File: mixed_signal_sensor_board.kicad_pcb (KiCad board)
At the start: 4 copper layers, 85 x 58 mm, 159 parts, among them J1 Conn_01x02, J10 Conn_01x04, J11 Conn_01x04, J12 Conn_01x04, J13 USB_C_Receptacle_USB2.0_16P, J14 Conn_01x04, J15 PYRO, J16 PYRO, J17 PYRO, J18 PYRO, J2 Conn_01x04, J3 Conn_01x06, J4 Conn_02x06_Odd_Even, J5 Conn_01x04, J6 Conn_01x04, J7 Conn_01x04, J8 Conn_01x04, J9 Conn_01x04, Q1 IRLML5103TRPBF, Q2 CSD17571Q2, Q3 CSD17571Q2, Q4 CSD17571Q2, Q5 CSD17571Q2, SW1 SW_Push, SW2 SW_Push, U1 TMP117xxDRV, U2 LM27762, U3 MagI3C_171013201, U4 TPS7A20xxxDBV, U5 TPS7A20xxxDBV, U6 ADS131M08xPBS, U7 STM32L552CEUx, U8 USBLC6-2P6, U9 TCAN3414DRBR, Y1 SG-8018CE_8.192M-TJHSA

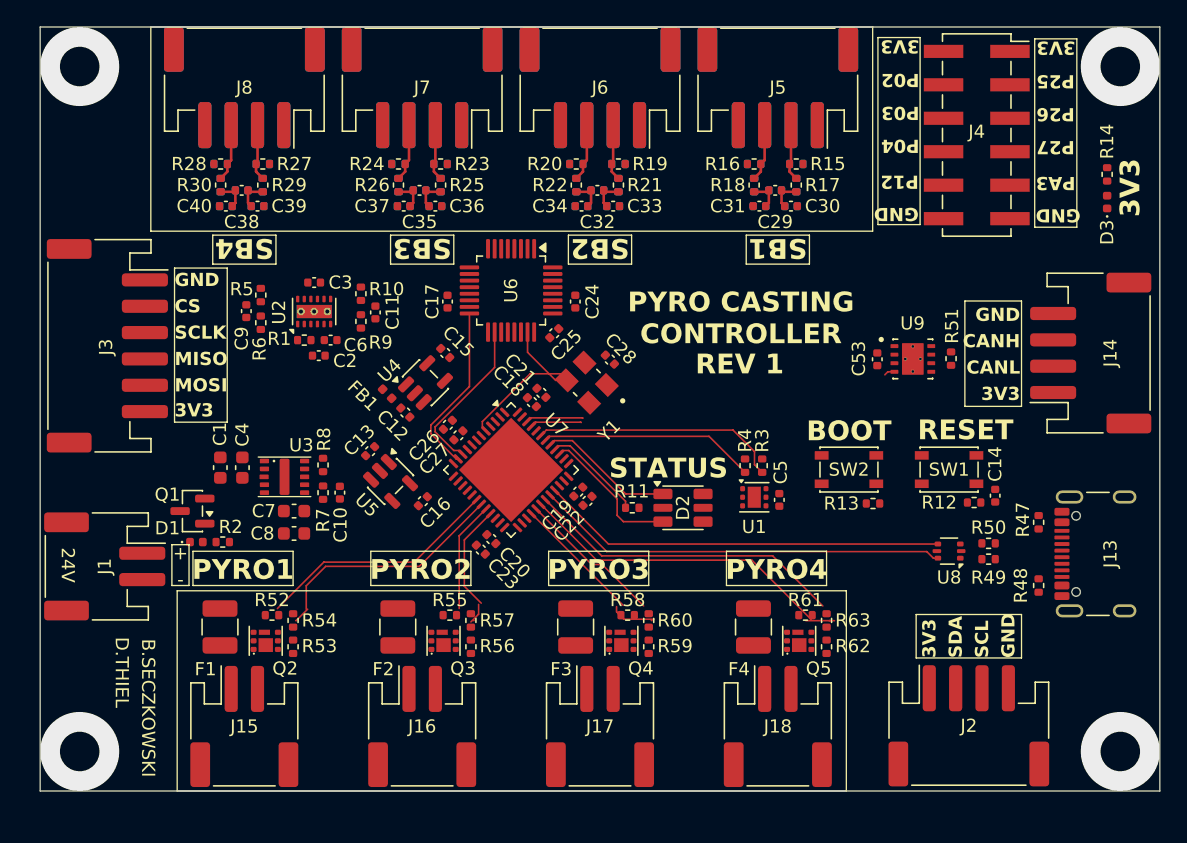
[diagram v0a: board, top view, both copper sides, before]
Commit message: removed SPI, I2C, compacting pyro channels, new pyro schematic
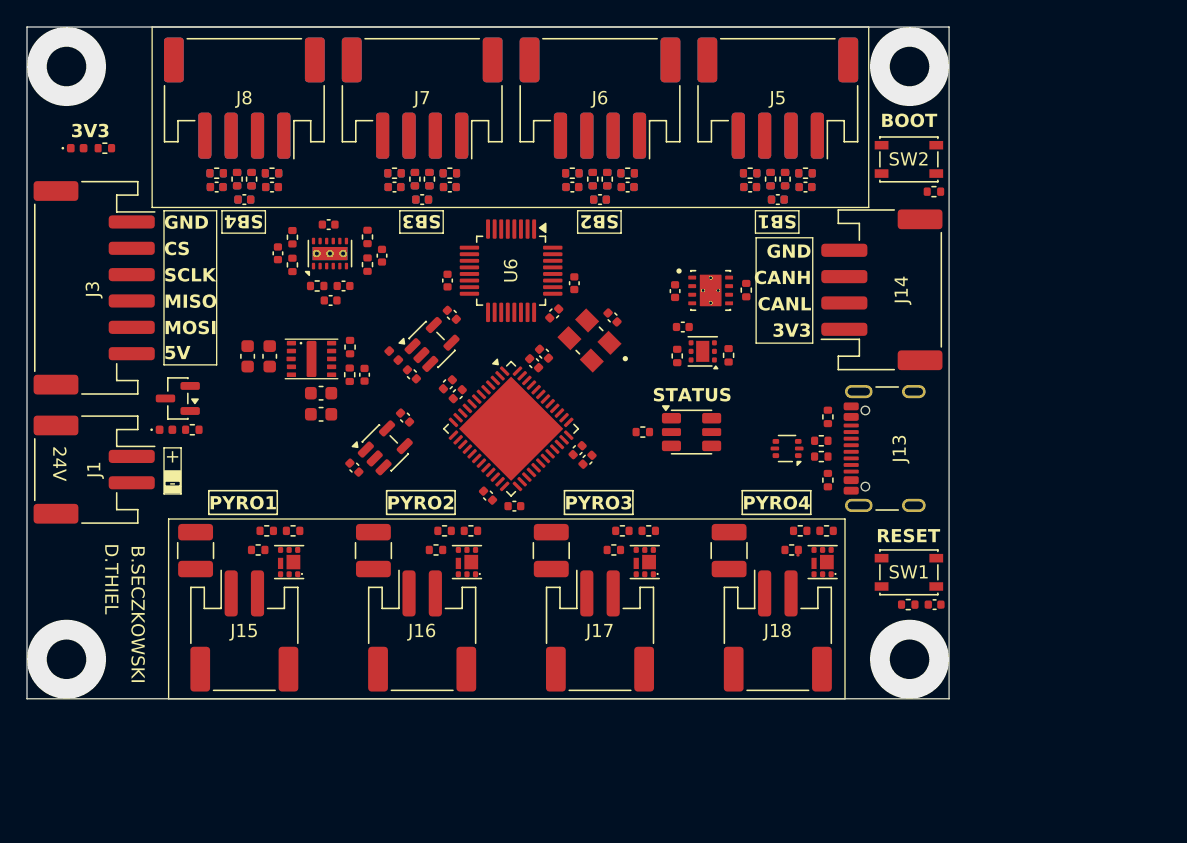
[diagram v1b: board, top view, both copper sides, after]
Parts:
- removed J2: Conn_01x04, Connector_JST:JST_PH_S4B-PH-SM4-TB_1x04-1MP_P2.00mm_Horizontal
- removed J4: Conn_02x06_Odd_Even, Connector_PinSocket_2.54mm:PinSocket_2x06_P2.54mm_Vertical_SMD
- moved D3 78.3 mm to (123.8, 61.2), turned to 0 degrees
- moved R14 76.1 mm to (125.9, 61.2), turned to 0 degrees
- moved R13 24.1 mm to (188.8, 64.5)
- moved SW2 24.0 mm to (186.9, 62.0)
- moved J13 17.9 mm to (186.2, 84.0)
- moved R47 17.9 mm to (180.8, 81.6)
- moved R48 17.9 mm to (180.8, 86.4)
- moved J14 16.6 mm to (184.9, 72.0)
- moved R51 16.4 mm to (174.6, 72.0)
- moved U9 16.2 mm to (171.9, 72.0)
- moved C53 16.2 mm to (169.2, 72.0)
- moved C5 15.0 mm to (169.8, 74.8), turned to 0 degrees
- moved R49 14.9 mm to (180.3, 84.6)
- moved R50 14.9 mm to (180.3, 83.4)
- moved U8 14.6 mm to (177.7, 84.0)
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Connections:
- U7 pad 10: /ADS_DRDY -> unconnected-(U7-PA0-Pad10)
- U7 pad 11: /ADS_SYNC/RESET -> unconnected-(U7-PA1-Pad11)
- U7 pad 12: /PA2 -> unconnected-(U7-PA2-Pad12)
- U7 pad 13: /PA3 -> unconnected-(U7-PA3-Pad13)
- U7 pad 2: /PC13 -> /ADS_DRDY
- U7 pad 25: /PB12 -> unconnected-(U7-PB12-Pad25)
- U7 pad 26: /PB13 -> unconnected-(U7-PB13-Pad26)
- U7 pad 27: /PB14 -> unconnected-(U7-PB14-Pad27)
- U7 pad 3: /PC14 -> /ADS_SYNC/RESET
- U7 pad 4: /PC15 -> unconnected-(U7-PC15-Pad4)
- U7 pad 5: /CLK_IN -> unconnected-(U7-PH0-Pad5)
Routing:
- net /USB_N: track 31.4 -> 0.00 mm
- net /USB_P: track 30.8 -> 0.00 mm
- net /PYRO4_FAULT: track 26.4 -> 0.00 mm
- net /PYRO4_SIGNAL: track 24.4 -> 0.06 mm
- net /PYRO1_FAULT: track 18.9 -> 0.00 mm
- net /SDA: track 18.9 -> 0.00 mm
- net /PYRO1_SIGNAL: track 18.6 -> 0.06 mm
- net /SCL: track 16.4 -> 0.00 mm
- net /CLK_IN: track 14.3 -> 0.00 mm
- net /PYRO3_FAULT: track 13.4 -> 0.00 mm
- net /ADS_SYNC/RESET: track 13.2 -> 0.00 mm
- net /ADS_DRDY: track 12.2 -> 0.00 mm
- net /PYRO3_SIGNAL: track 11.2 -> 0.06 mm
- net /LEDG: track 10.9 -> 0.00 mm
- net /LEDB: track 10.4 -> 0.00 mm
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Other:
- board size 85 x 58 mm -> 70 x 51 mm
- board text added: "5V"
- board text removed: "P02"
- board text removed: "P03"
- board text removed: "P04"
- board text removed: "P12"
- board text removed: "P25"
- board text removed: "P26"
- board text removed: "P27"
- board text removed: "PA3"
- board text removed: "PYRO CASTING CONTROLLER"
- board text removed: "REV 1"
- board text removed: "SCL"
- board text removed: "SDA"

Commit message: New pyro layout, SWDIO, SWCLK, USART2 TX RX, 70x50mm board
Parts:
- removed F1, F2, F3, F4: Polyfuse, Fuse:Fuse_1210_3225Metric
- removed J15, J16, J17, J18: PYRO, Connector_JST:JST_PH_S2B-PH-SM4-TB_1x02-1MP_P2.00mm_Horizontal
- removed R52, R54, R55, R57, R58, R60, R61, R63: 10K, Resistor_SMD:R_0402_1005Metric
- removed R53, R56, R59, R62: 70K, Resistor_SMD:R_0402_1005Metric
- added 50k1: 10K, Resistor_SMD:R_0402_1005Metric, F.Cu at (147.6, 92.2)
- added D4: 3V, Diode_SMD:D_0402_1005Metric, F.Cu at (149.3, 96.2)
- added D5: 3V, Diode_SMD:D_0402_1005Metric, F.Cu at (159.8, 96.2)
- added D6: 3V, Diode_SMD:D_0402_1005Metric, F.Cu at (170.3, 96.2)
- added D7: 3V, Diode_SMD:D_0402_1005Metric, F.Cu at (180.8, 96.2)
- added F5: Polyfuse, Fuse:Fuse_1210_3225Metric, F.Cu at (140.6, 90.7)
- added F6: Polyfuse, Fuse:Fuse_1210_3225Metric, F.Cu at (151.1, 90.7)
- added F7: Polyfuse, Fuse:Fuse_1210_3225Metric, F.Cu at (161.6, 90.7)
- added F8: Polyfuse, Fuse:Fuse_1210_3225Metric, F.Cu at (172.1, 90.7)
- added J19: PYRO, Connector_JST:JST_PH_S2B-PH-SM4-TB_1x02-1MP_P2.00mm_Horizontal, F.Cu at (144.2, 96.8)
- added J20: PYRO, Connector_JST:JST_PH_S2B-PH-SM4-TB_1x02-1MP_P2.00mm_Horizontal, F.Cu at (154.8, 96.8)
- added J21: PYRO, Connector_JST:JST_PH_S2B-PH-SM4-TB_1x02-1MP_P2.00mm_Horizontal, F.Cu at (165.2, 96.8)
- added J22: PYRO, Connector_JST:JST_PH_S2B-PH-SM4-TB_1x02-1MP_P2.00mm_Horizontal, F.Cu at (175.8, 96.8)
- added J23: PYRO_ARM, Connector_JST:JST_PH_S2B-PH-SM4-TB_1x02-1MP_P2.00mm_Horizontal, F.Cu at (133.8, 96.8)
- added Q10: CSD17571Q2, CSD17571Q2:CSD17571Q2, F.Cu at (147.8, 90.2)
- added Q11: CSD17571Q2, CSD17571Q2:CSD17571Q2, F.Cu at (158.3, 90.2)
- added Q12: CSD17571Q2, CSD17571Q2:CSD17571Q2, F.Cu at (168.8, 90.2)
- added Q13: CSD17571Q2, CSD17571Q2:CSD17571Q2, F.Cu at (179.3, 90.2)
- added R72: 50K, Resistor_SMD:R_0402_1005Metric, F.Cu at (149.3, 94.0)
- added R74: 50K, Resistor_SMD:R_0402_1005Metric, F.Cu at (159.8, 94.0)
- added R75: 10K, Resistor_SMD:R_0402_1005Metric, F.Cu at (158.1, 92.2)
- added R76: 50K, Resistor_SMD:R_0402_1005Metric, F.Cu at (170.3, 94.0)
- added R77: 10K, Resistor_SMD:R_0402_1005Metric, F.Cu at (168.6, 92.2)
- added R78: 50K, Resistor_SMD:R_0402_1005Metric, F.Cu at (180.8, 94.0)
- added R79: 10K, Resistor_SMD:R_0402_1005Metric, F.Cu at (179.1, 92.2)
- added R80: 100k, Resistor_SMD:R_0402_1005Metric, F.Cu at (147.5, 88.2)
- added R81: 100k, Resistor_SMD:R_0402_1005Metric, F.Cu at (158.0, 88.2)
- added R82: 100k, Resistor_SMD:R_0402_1005Metric, F.Cu at (168.5, 88.2)
- added R83: 100k, Resistor_SMD:R_0402_1005Metric, F.Cu at (179.0, 88.2)
- D1: value 30V -> 24V
- Q2, Q3, Q4, Q5: value CSD17571Q2 -> IRLML5103TRPBF; footprint CSD17571Q2:CSD17571Q2 -> Package_TO_SOT_SMD:SOT-23
- moved D3 48.7 mm to (171.9, 68.6), turned to 180 degrees
- moved R14 44.6 mm to (169.9, 68.6)
- moved C14 7.27 mm to (184.7, 90.0), turned to 180 degrees
- moved R12 5.91 mm to (186.7, 90.0), turned to 180 degrees
- moved D1 5.64 mm to (132.9, 87.7)
- moved R2 5.64 mm to (134.9, 87.7)
- moved Q5 5.55 mm to (175.8, 89.6), turned to -90 degrees
- moved Q2 5.30 mm to (144.2, 89.6), turned to -90 degrees
- moved C13 4.34 mm to (147.3, 81.9), turned to 90 degrees
- moved Q1 4.05 mm to (133.8, 83.5)
- moved C16 4.01 mm to (152.7, 81.9), turned to -90 degrees
- moved C20 3.93 mm to (158.2, 85.3)
- moved U7 3.87 mm to (160.0, 80.4)
- moved C26 3.86 mm to (155.2, 77.0)
- moved C27 3.86 mm to (155.9, 77.8)
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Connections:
- D1 pad 1: Net-(D1-K) -> +24V
- J1 pad 1: Net-(D1-K) -> Net-(J1-Pin_1)
- J3 pad 2: /MOSI -> /USART2_TX
- J3 pad 3: /MISO -> /USART2_RX
- J3 pad 4: /SCLK -> /SWDIO
- J3 pad 5: /CS -> /SWCLK
- J3 pad 6: +3V3 -> +5V
- Q1 pad 3: Net-(D1-K) -> Net-(J1-Pin_1)
- U7 pad 12: unconnected-(U7-PA2-Pad12) -> /USART2_TX
- U7 pad 13: unconnected-(U7-PA3-Pad13) -> /USART2_RX
- U7 pad 34: unconnected-(U7-PA13-Pad34) -> /SWDIO
- U7 pad 37: unconnected-(U7-PA14-Pad37) -> /SWCLK
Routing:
- net GND: track 2.96 -> 2.14 mm
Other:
- board size 70 x 51 mm -> 70 x 50 mm
- board text added: "ARM"
- board text added: "P12"
- board text added: "P13"
- board text added: "P34"
- board text added: "P37"
- board text removed: "5V"
- board text removed: "CS"
- board text removed: "MISO"
- board text removed: "MOSI"
- board text removed: "SCLK"

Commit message: PYRO done, schematic structure/convention update, pyro and reverse polarity components selected
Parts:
- removed Q1: IRLML5103TRPBF, Package_TO_SOT_SMD:SOT-23
- removed Q11, Q12, Q13: CSD17571Q2, CSD17571Q2:CSD17571Q2
- added Q2: 2N7002WT1G, Package_TO_SOT_SMD:SOT-323_SC-70, F.Cu at (147.4, 90.3)
- added Q4: 2N7002WT1G, Package_TO_SOT_SMD:SOT-323_SC-70, F.Cu at (157.9, 90.3)
- added Q6: 2N7002WT1G, Package_TO_SOT_SMD:SOT-323_SC-70, F.Cu at (168.4, 90.3)
- added Q8: 2N7002WT1G, Package_TO_SOT_SMD:SOT-323_SC-70, F.Cu at (178.9, 90.3)
- added R52: 10k, Resistor_SMD:R_0402_1005Metric, F.Cu at (137.8, 83.3)
- added R53: 1k, Resistor_SMD:R_0402_1005Metric, F.Cu at (137.8, 85.3)
- added R55: 1k, Resistor_SMD:R_0402_1005Metric, F.Cu at (144.3, 88.1)
- added R58: 10k, Resistor_SMD:R_0402_1005Metric, F.Cu at (162.0, 107.5)
- added R59: 1k, Resistor_SMD:R_0402_1005Metric, F.Cu at (162.0, 109.5)
- added R61: 1k, Resistor_SMD:R_0402_1005Metric, F.Cu at (162.0, 111.5)
- added R64: 10k, Resistor_SMD:R_0402_1005Metric, F.Cu at (166.9, 107.5)
- added R65: 1k, Resistor_SMD:R_0402_1005Metric, F.Cu at (166.9, 109.5)
- added R67: 1k, Resistor_SMD:R_0402_1005Metric, F.Cu at (166.9, 111.5)
- added R70: 10k, Resistor_SMD:R_0402_1005Metric, F.Cu at (157.1, 107.5)
- added R71: 1k, Resistor_SMD:R_0402_1005Metric, F.Cu at (157.1, 109.5)
- added R73: 1k, Resistor_SMD:R_0402_1005Metric, F.Cu at (157.1, 111.5)
- F1: renamed from F5; value Polyfuse -> MF-USHT050KX-2
- F2: renamed from F6; value Polyfuse -> MF-USHT050KX-2
- F3: renamed from F7; value Polyfuse -> MF-USHT050KX-2
- F4: renamed from F8; value Polyfuse -> MF-USHT050KX-2
- Q10: value CSD17571Q2 -> SQA405EJ-T1_GE3; footprint CSD17571Q2:CSD17571Q2 -> Package_TO_SOT_SMD:Vishay_PowerPAK_SC70-6L_Single
- Q3: renamed from Q2; value IRLML5103TRPBF -> SQA405EJ-T1_GE3; footprint Package_TO_SOT_SMD:SOT-23 -> Package_TO_SOT_SMD:Vishay_PowerPAK_SC70-6L_Single
- Q5: renamed from Q3; value IRLML5103TRPBF -> SQA405EJ-T1_GE3; footprint Package_TO_SOT_SMD:SOT-23 -> Package_TO_SOT_SMD:Vishay_PowerPAK_SC70-6L_Single
- Q7: renamed from Q4; value IRLML5103TRPBF -> SQA405EJ-T1_GE3; footprint Package_TO_SOT_SMD:SOT-23 -> Package_TO_SOT_SMD:Vishay_PowerPAK_SC70-6L_Single
- Q9: renamed from Q5; value IRLML5103TRPBF -> SQA405EJ-T1_GE3; footprint Package_TO_SOT_SMD:SOT-23 -> Package_TO_SOT_SMD:Vishay_PowerPAK_SC70-6L_Single
- R54: renamed from R80; value 100k -> 10k
- R56: renamed from 50k1; value 10K -> 50k
- R57: renamed from R72; value 50K -> 50k
- R60: renamed from R81; value 100k -> 10k
- R62: renamed from R75; value 10K -> 50k
- R63: renamed from R74; value 50K -> 50k
- R66: renamed from R82; value 100k -> 10k
- R68: renamed from R77; value 10K -> 50k
- R69: renamed from R76; value 50K -> 50k
- R72: renamed from R83; value 100k -> 10k
- R74: renamed from R79; value 10K -> 50k
- R75: renamed from R78; value 50K -> 50k
- moved Q10 15.5 mm to (133.8, 83.7), turned to 90 degrees
- moved R2 2.20 mm to (132.7, 87.7), turned to 180 degrees
- moved D1 1.80 mm to (134.7, 87.7), turned to 180 degrees
- moved Q3 0.51 mm to (144.2, 90.1)
- moved R56 0.25 mm to (147.3, 92.4)
- moved R62 0.25 mm to (157.8, 92.4)
- moved R68 0.25 mm to (168.3, 92.4)
- moved R74 0.25 mm to (178.8, 92.4)
- moved Q5 0.21 mm to (154.8, 89.8)
- moved Q7 0.21 mm to (165.2, 89.8)
- moved Q9 0.21 mm to (175.8, 89.8)
- moved R54 0.12 mm to (147.4, 88.2)
- moved R60 0.12 mm to (157.9, 88.2)
- moved R66 0.12 mm to (168.4, 88.2)
- moved R72 0.12 mm to (178.9, 88.2)
- renumbered J11 to J10, J12 to J11, J13 to J12, J14 to J13, J19 to J14, J20 to J15, J21 to J16, J22 to J17, J23 to J2, J5 to J4, J6 to J5, J7 to J6, J8 to J7, J9 to J8, J10 to J9
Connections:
- F1 pad 1: Net-(Q2-S) -> Net-(Q3-S)
- F2 pad 1: Net-(Q3-S) -> Net-(Q5-S)
- F3 pad 1: Net-(Q4-S) -> Net-(Q7-S)
- F4 pad 1: Net-(Q5-S) -> Net-(Q9-S)
- J3 pad 6: +5V -> +5V5
- Q10 pad 1: /PYRO1_SIGNAL -> Net-(J1-Pin_1)
- Q10 pad 3: Net-(Q10-D) -> Net-(D1-A)
- Q3 pad 1: Net-(Q10-D) -> ARM
- Q3 pad 3: ARM -> Net-(Q3-G)
- Q5 pad 1: Net-(Q11-D) -> ARM
- Q5 pad 3: ARM -> Net-(Q5-G)
- Q7 pad 1: Net-(Q12-D) -> ARM
- Q7 pad 3: ARM -> Net-(Q7-G)
- Q9 pad 1: Net-(Q13-D) -> ARM
- Q9 pad 3: ARM -> Net-(Q9-G)
- R54 pad 2: Net-(Q10-D) -> Net-(Q2-D)
- R60 pad 2: Net-(Q11-D) -> Net-(Q4-D)
- R66 pad 2: Net-(Q12-D) -> Net-(Q6-D)
- R72 pad 2: Net-(Q13-D) -> Net-(Q8-D)
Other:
- board text added: "5V5"
